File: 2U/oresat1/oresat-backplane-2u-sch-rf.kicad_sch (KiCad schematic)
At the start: 8 parts

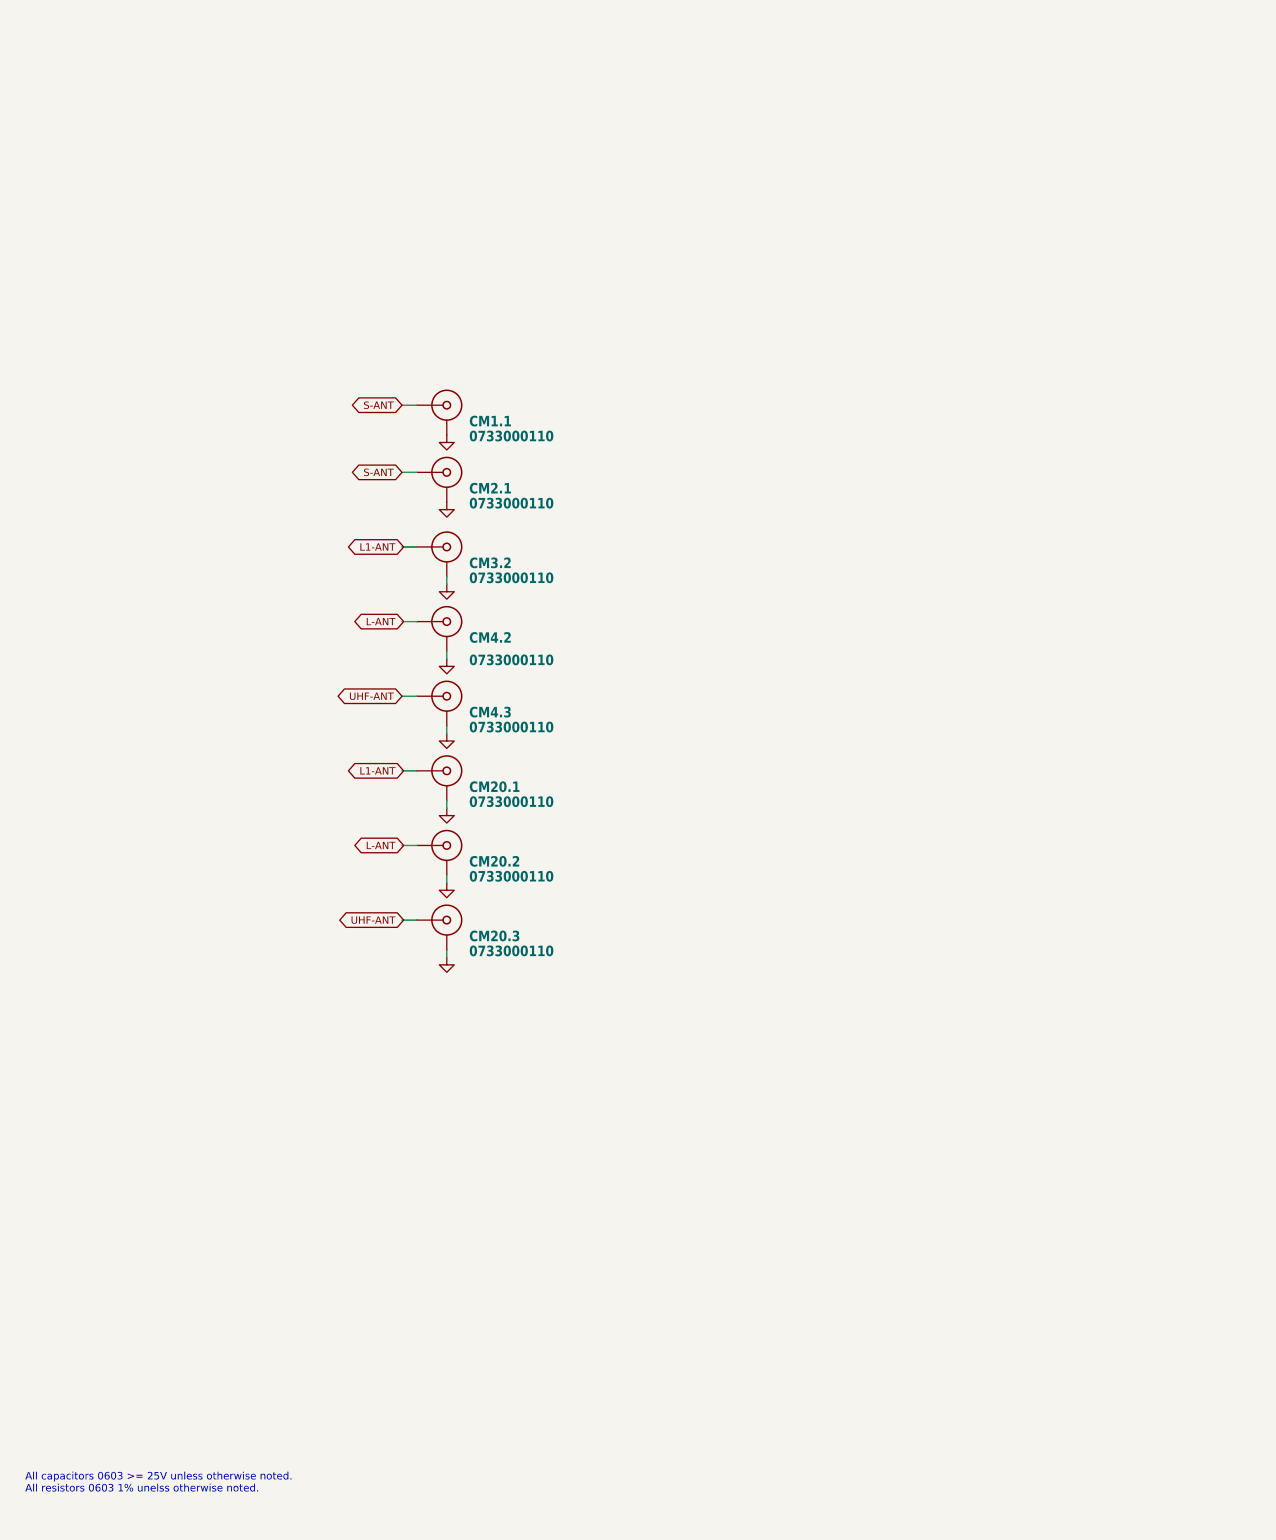
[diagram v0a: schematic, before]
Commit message: Update of OreSat1 2U backplane. Removed extraneous connectors, imported DXF from OnShape and moved debug connectors by 0.176 mm. Routing left to do.
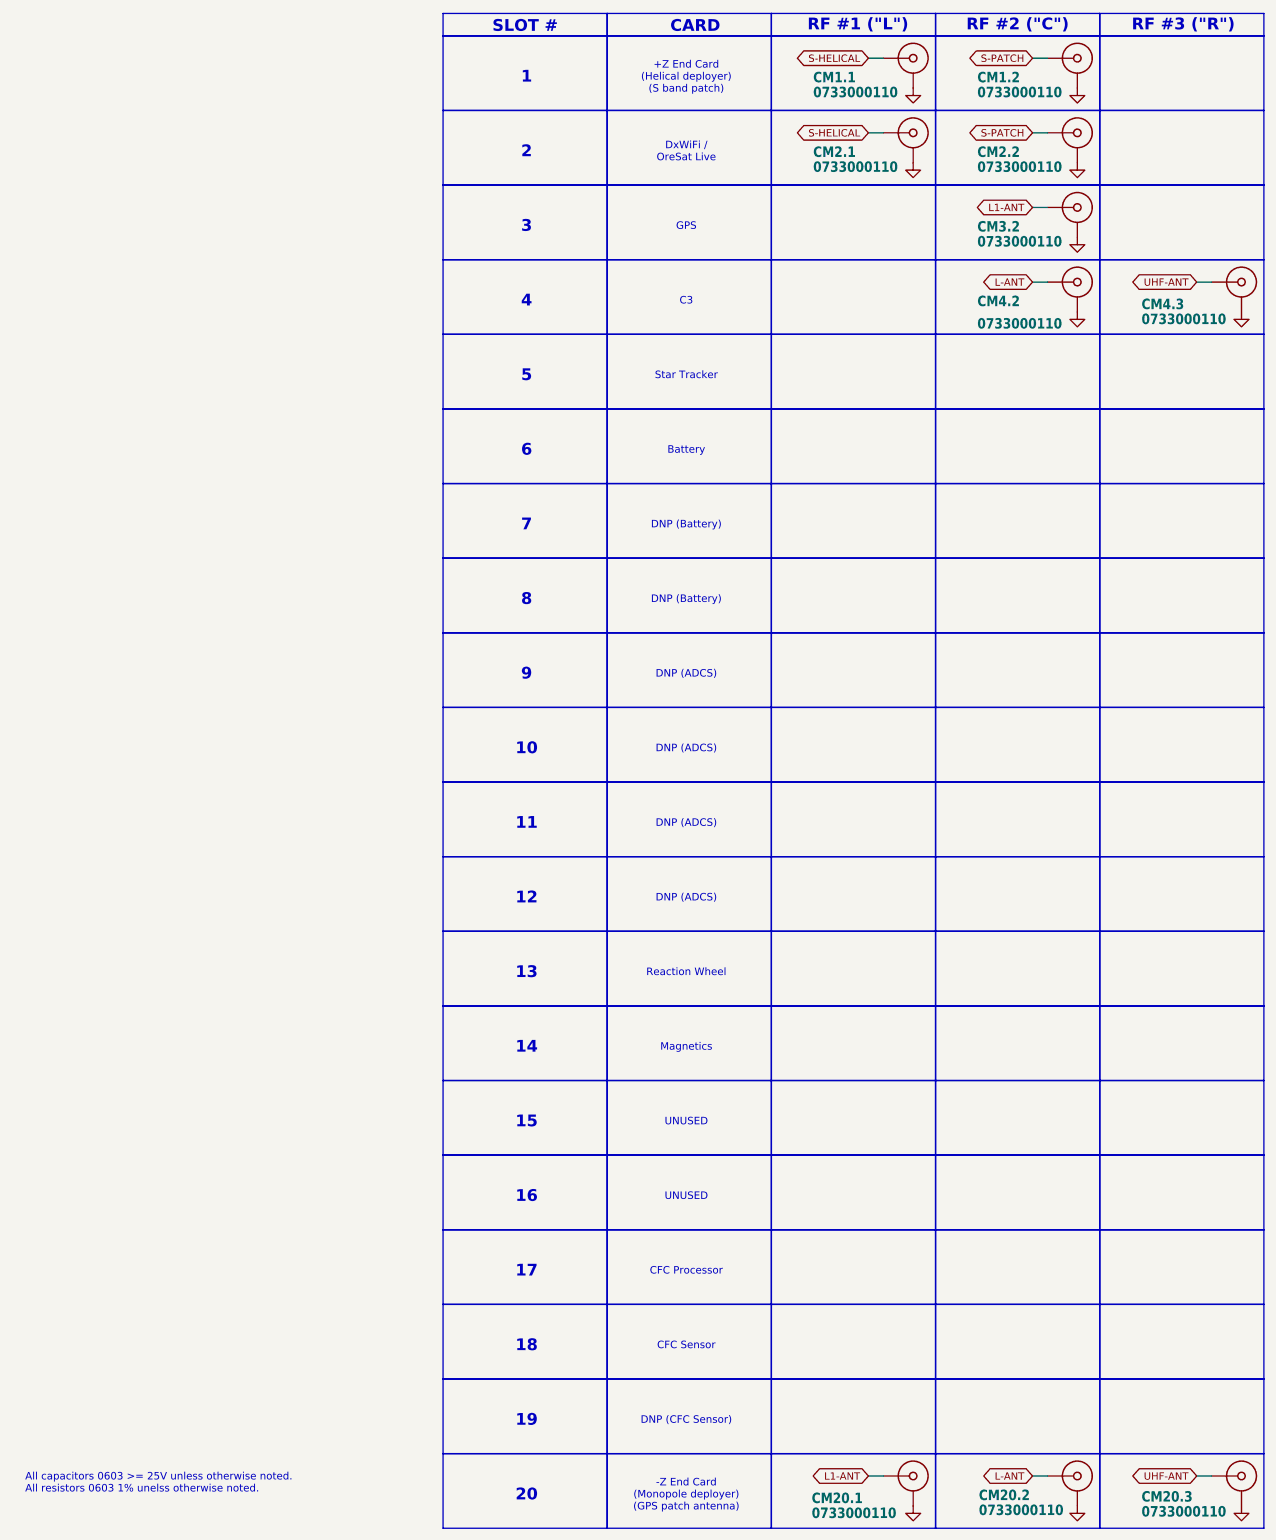
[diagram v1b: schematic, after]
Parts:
- added CM1.2, CM2.2: 0733000110, oresat-connectors:J-MOLEX-SMPM-73300-0111X-long, symbol oresat-connectors:J-MOLEX-SMPM-73300-0111X_1
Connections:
- net GND: now also CM1.2.GND (SHIELD1), CM2.2.GND (SHIELD1)
- net S-ANT renamed S-HELICAL
- new net S-PATCH: CM1.2.RF-DOWN (RF), CM2.2.RF-DOWN (RF)
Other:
- note added: "+Z End Card (Helical deployer) (S band patch)"
- note added: "-Z End Card (Monopole deployer) (GPS patch antenna)"
- note added: "1"
- note added: "10"
- note added: "11"
- note added: "12"
- note added: "13"
- note added: "14"
- note added: "15"
- note added: "16"
- note added: "17"
- note added: "18"
- note added: "19"
- note added: "2"
- note added: "20"
- note added: "3"
- note added: "4"
- note added: "5"
- note added: "6"
- note added: "7"
- note added: "8"
- note added: "9"
- note added: "Battery"
- note added: "C3"
- note added: "CARD"
- note added: "CFC Processor"
- note added: "CFC Sensor"
- note added: "DNP (ADCS)"
- note added: "DNP (Battery)"
- note added: "DNP (CFC Sensor)"
- note added: "DxWiFi / OreSat Live"
- note added: "GPS"
- note added: "Magnetics"
- note added: "RF #1 ("L")"
- note added: "RF #2 ("C")"
- note added: "RF #3 ("R")"
- note added: "Reaction Wheel"
- note added: "SLOT #"
- note added: "Star Tracker"
- note added: "UNUSED"
- moved on the sheet: CM1.1, CM2.1, CM20.1, CM20.2, CM20.3, CM3.2, CM4.2, CM4.3

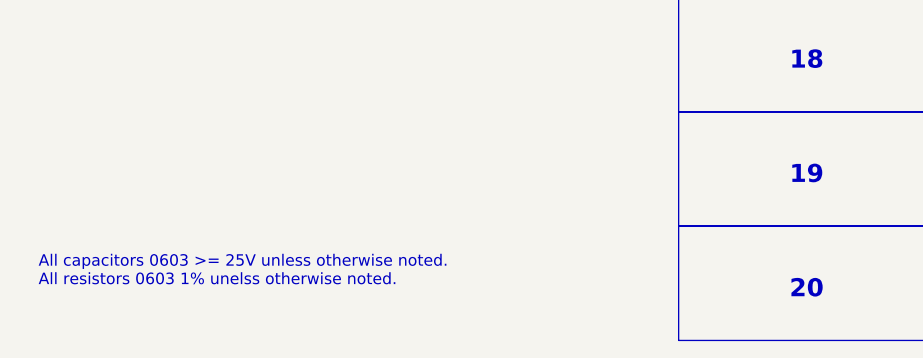
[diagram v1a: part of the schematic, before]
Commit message: Final fix and polish on 2U backplane for OreSat1.
Found a bunch of small little details to fix - somehow CAN lines were down to 0.2 mm, fixed to 0.3 mm. Also expanded some of
the lines to 0.6 mm for higher power lines. Added more vias for VBUS on the debug connector, and finally added 3D models
to all of the connectors so the backplane fully renders now!
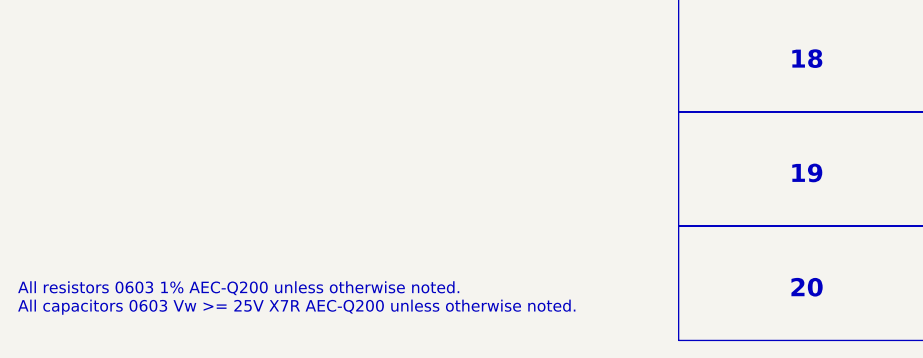
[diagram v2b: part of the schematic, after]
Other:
- note added: "All resistors 0603 1% AEC-Q200 unless otherwise noted. All capacitors 0603 Vw >= 25V X7R AEC-Q200 unless otherwise noted."
- note removed: "All capacitors 0603 >= 25V unless otherwise noted. All resistors 0603 1% unelss otherwise noted."
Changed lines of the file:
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@@
 	(title_block
 		(title "OreSat1 2U Backplane")
-		(date "2025-09-28")
+		(date "2025-11-30")
 		(rev "1.0")
 		(company "Portland State Aerospace Society")
@@
 		)
 	)
-	(text "All capacitors 0603 >= 25V unless otherwise noted.\nAll resistors 0603 1% unelss otherwise noted."
-		(exclude_from_sim no)
-		(at 115.57 261.62 0)
+	(text "RF #2 (\"C\")"
+		(exclude_from_sim no)
+		(at 284.48 13.462 0)
+		(effects
+			(font
+				(size 2 2)
+				(thickness 0.4)
+				(bold yes)
+			)
+		)
+	)
+	(text "18"
+		(exclude_from_sim no)
+		(at 200.914 238.252 0)
+		(effects
+			(font
+				(size 2 2)
+				(thickness 0.4)
+				(bold yes)
+			)
+		)
+	)
+	(text "DNP (Battery)"
+		(exclude_from_sim no)
+		(at 228.092 98.552 0)
+		(effects
+			(font
+				(size 1.27 1.27)
+			)
+		)
+	)
+	(text "Reaction Wheel"
+		(exclude_from_sim no)
+		(at 228.092 174.752 0)
+		(effects
+			(font
+				(size 1.27 1.27)
+			)
+		)
+	)
+	(text "DNP (ADCS)"
+		(exclude_from_sim no)
+		(at 228.092 162.052 0)
+		(effects
+			(font
+				(size 1.27 1.27)
+			)
+		)
+	)
+	(text "3"
+		(exclude_from_sim no)
+		(at 200.914 47.752 0)
+		(effects
+			(font
+				(size 2 2)
+				(thickness 0.4)
+				(bold yes)
+			)
+		)
+	)
+	(text "16"
+		(exclude_from_sim no)
+		(at 200.914 212.852 0)
+		(effects
+			(font
+				(size 2 2)
+				(thickness 0.4)
+				(bold yes)
+			)
+		)
+	)
+	(text "DNP (ADCS)"
+		(exclude_from_sim no)
+		(at 228.092 136.652 0)
+		(effects
+			(font
+				(size 1.27 1.27)
+			)
+		)
+	)
+	(text "DNP (ADCS)"
+		(exclude_from_sim no)
+		(at 228.092 149.352 0)
+		(effects
+			(font
+				(size 1.27 1.27)
+			)
+		)
+	)
+	(text "All resistors 0603 1% AEC-Q200 unless otherwise noted.\nAll capacitors 0603 Vw >= 25V X7R AEC-Q200 unless otherwise noted.\n"
+		(exclude_from_sim no)
+		(at 113.284 264.668 0)
 		(effects
 			(font
@@
 		)
 	)
-	(text "RF #2 (\"C\")"
-		(exclude_from_sim no)
-		(at 284.48 13.462 0)
-		(effects
-			(font
-				(size 2 2)
-				(thickness 0.4)
-				(bold yes)
-			)
-		)
-	)
-	(text "18"
-		(exclude_from_sim no)
-		(at 200.914 238.252 0)
-		(effects
-			(font
-				(size 2 2)
-				(thickness 0.4)
-				(bold yes)
-			)
-		)
-	)
-	(text "DNP (Battery)"
-		(exclude_from_sim no)
-		(at 228.092 98.552 0)
-		(effects
-			(font
-				(size 1.27 1.27)
-			)
-		)
-	)
-	(text "Reaction Wheel"
-		(exclude_from_sim no)
-		(at 228.092 174.752 0)
-		(effects
-			(font
-				(size 1.27 1.27)
-			)
-		)
-	)
-	(text "DNP (ADCS)"
-		(exclude_from_sim no)
-		(at 228.092 162.052 0)
-		(effects
-			(font
-				(size 1.27 1.27)
-			)
-		)
-	)
-	(text "3"
-		(exclude_from_sim no)
-		(at 200.914 47.752 0)
-		(effects
-			(font
-				(size 2 2)
-				(thickness 0.4)
-				(bold yes)
-			)
-		)
-	)
-	(text "16"
-		(exclude_from_sim no)
-		(at 200.914 212.852 0)
-		(effects
-			(font
-				(size 2 2)
-				(thickness 0.4)
-				(bold yes)
-			)
-		)
-	)
-	(text "DNP (ADCS)"
-		(exclude_from_sim no)
-		(at 228.092 136.652 0)
-		(effects
-			(font
-				(size 1.27 1.27)
-			)
-		)
-	)
-	(text "DNP (ADCS)"
-		(exclude_from_sim no)
-		(at 228.092 149.352 0)
-		(effects
-			(font
-				(size 1.27 1.27)
-			)
-		)
-	)
